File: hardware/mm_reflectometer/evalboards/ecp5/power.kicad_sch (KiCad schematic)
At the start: 49 parts, among them U101 ECP5U_25_CABGA256, U201 TLV70025_WSON6, U202 TLV62569DRL, U203 TLV62569DRL, U204 TLV70018_WSON6, U205 LM3880MF-1AF, U206 LT3494

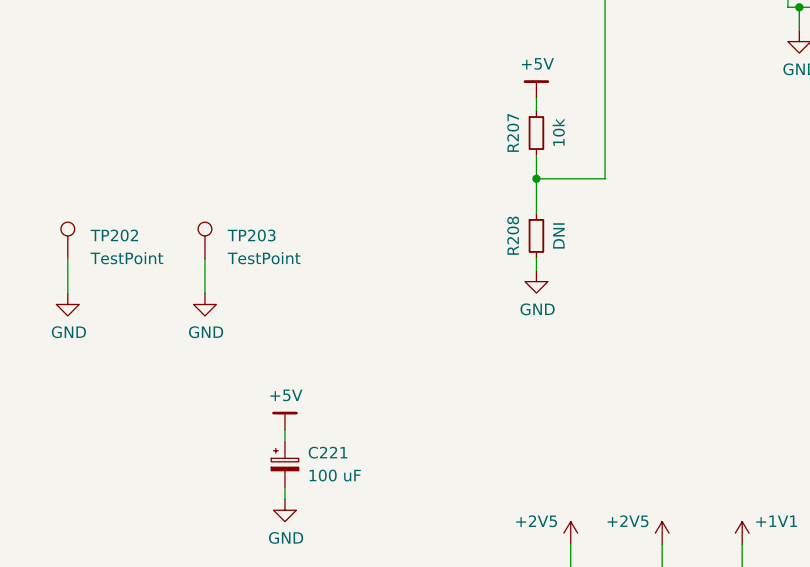
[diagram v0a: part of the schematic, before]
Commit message: all nets routed on ecp5 eval board
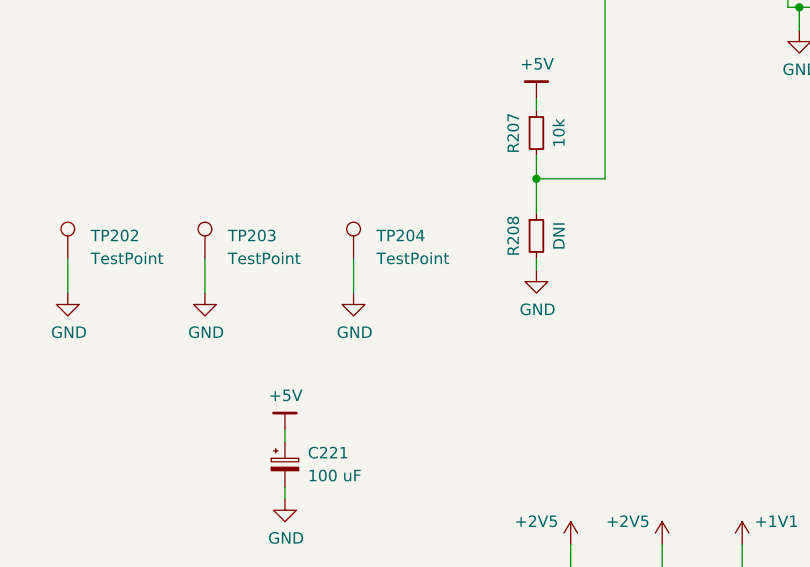
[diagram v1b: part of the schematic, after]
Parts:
- added TP204: TestPoint, TestPoint:TestPoint_Keystone_5015_Micro-Minature, symbol Connector:TestPoint
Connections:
- net GND: now also TP204.1
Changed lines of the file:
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@@
+    (stroke (width 0) (type solid) (color 0 0 0 0))
+  )
+  (wire (pts (xy 181.61 80.01) (xy 181.61 83.82))
     (stroke (width 0) (type solid) (color 0 0 0 0))
   )
@@
     )
   )
+  (symbol (lib_id "Connector:TestPoint") (at 181.61 80.01 0) (unit 1)
+    (in_bom yes) (on_board yes)
+    (property "Reference" "TP204" (id 0) (at 184.15 77.47 0)
+      (effects (font (size 1.27 1.27)) (justify left))
+    )
+    (property "Value" "TestPoint" (id 1) (at 184.15 80.01 0)
+      (effects (font (size 1.27 1.27)) (justify left))
+    )
+    (property "Footprint" "TestPoint:TestPoint_Keystone_5015_Micro-Minature" (id 2) (at 186.69 80.01 0)
+      (effects (font (size 1.27 1.27)) hide)
+    )
+    (property "Datasheet" "~" (id 3) (at 186.69 80.01 0)
+      (effects (font (size 1.27 1.27)) hide)
+    )
+  )
   (symbol (lib_id "power:+3V3") (at 26.67 52.07 0) (unit 1)
     (in_bom yes) (on_board yes)
@@
       (effects (font (size 1.27 1.27)) hide)
     )
+  )
+  (symbol (lib_id "power:GND") (at 181.61 83.82 0) (unit 1)
+    (in_bom yes) (on_board yes)
+    (property "Reference" "#PWR0245" (id 0) (at 181.61 90.17 0)
+      (effects (font (size 1.27 1.27)) hide)
+    )
+    (property "Value" "GND" (id 1) (at 181.737 88.2142 0))
+    (property "Footprint" "" (id 2) (at 181.61 83.82 0)
+      (effects (font (size 1.27 1.27)) hide)
+    )
+    (property "Datasheet" "" (id 3) (at 181.61 83.82 0)
+      (effects (font (size 1.27 1.27)) hide)
+    )

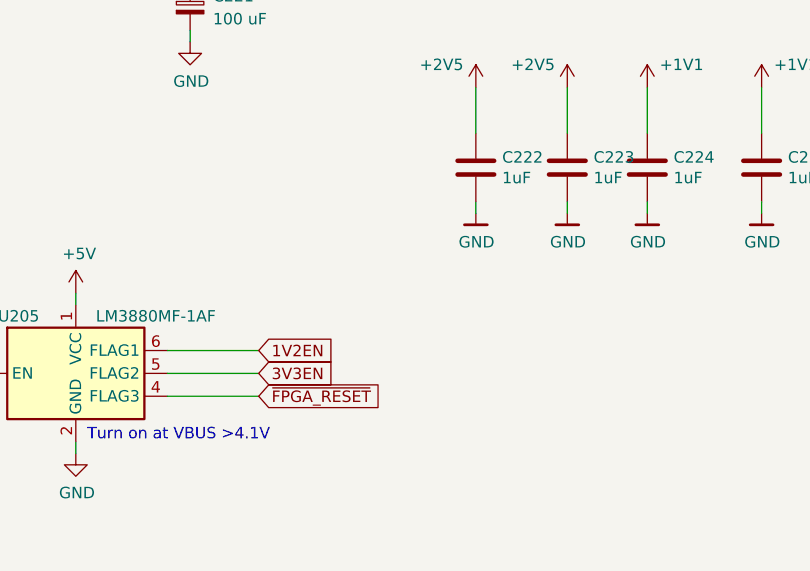
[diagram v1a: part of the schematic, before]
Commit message: cleanup ecp5 schematic, generated assembly drawings
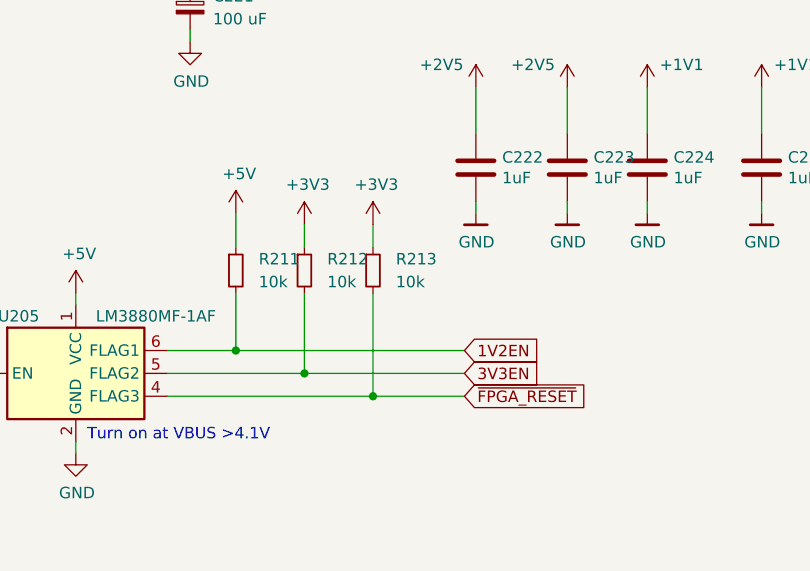
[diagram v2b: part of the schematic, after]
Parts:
- added R211, R212, R213: 10k, Resistor_SMD:R_0402_1005Metric, symbol Device:R_Small
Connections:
- net +3V3: now also R212.1, R213.1
- net +5V: now also R211.1
- net 1V2EN: now also R211.2
- net 3V3EN: now also R212.2
- net ~FPGA_RESET: now also R213.2
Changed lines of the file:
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@@
   (junction (at 153.67 34.29) (diameter 0.9144) (color 0 0 0 0))
   (junction (at 177.8 34.29) (diameter 0.9144) (color 0 0 0 0))
+  (junction (at 179.07 140.97) (diameter 0.9144) (color 0 0 0 0))
   (junction (at 186.69 34.29) (diameter 0.9144) (color 0 0 0 0))
+  (junction (at 186.69 143.51) (diameter 0.9144) (color 0 0 0 0))
+  (junction (at 194.31 146.05) (diameter 0.9144) (color 0 0 0 0))
   (junction (at 196.85 34.29) (diameter 0.9144) (color 0 0 0 0))
   (junction (at 201.93 71.12) (diameter 0.9144) (color 0 0 0 0))
@@
     (stroke (width 0) (type solid) (color 0 0 0 0))
   )
-  (wire (pts (xy 171.45 140.97) (xy 181.61 140.97))
-    (stroke (width 0) (type solid) (color 0 0 0 0))
-  )
-  (wire (pts (xy 171.45 143.51) (xy 181.61 143.51))
-    (stroke (width 0) (type solid) (color 0 0 0 0))
-  )
-  (wire (pts (xy 171.45 146.05) (xy 181.61 146.05))
+  (wire (pts (xy 171.45 140.97) (xy 179.07 140.97))
+    (stroke (width 0) (type solid) (color 0 0 0 0))
+  )
+  (wire (pts (xy 171.45 143.51) (xy 186.69 143.51))
+    (stroke (width 0) (type solid) (color 0 0 0 0))
+  )
+  (wire (pts (xy 171.45 146.05) (xy 194.31 146.05))
     (stroke (width 0) (type solid) (color 0 0 0 0))
   )
@@
     (stroke (width 0) (type solid) (color 0 0 0 0))
   )
+  (wire (pts (xy 179.07 125.73) (xy 179.07 129.54))
+    (stroke (width 0) (type solid) (color 0 0 0 0))
+  )
+  (wire (pts (xy 179.07 134.62) (xy 179.07 140.97))
+    (stroke (width 0) (type solid) (color 0 0 0 0))
+  )
+  (wire (pts (xy 179.07 140.97) (xy 204.47 140.97))
+    (stroke (width 0) (type solid) (color 0 0 0 0))
+  )
   (wire (pts (xy 181.61 80.01) (xy 181.61 83.82))
     (stroke (width 0) (type solid) (color 0 0 0 0))
@@
   )
   (wire (pts (xy 186.69 41.91) (xy 186.69 45.72))
+    (stroke (width 0) (type solid) (color 0 0 0 0))
+  )
+  (wire (pts (xy 186.69 127) (xy 186.69 129.54))
+    (stroke (width 0) (type solid) (color 0 0 0 0))
+  )
+  (wire (pts (xy 186.69 134.62) (xy 186.69 143.51))
+    (stroke (width 0) (type solid) (color 0 0 0 0))
+  )
+  (wire (pts (xy 186.69 143.51) (xy 204.47 143.51))
+    (stroke (width 0) (type solid) (color 0 0 0 0))
+  )
+  (wire (pts (xy 194.31 127) (xy 194.31 129.54))
+    (stroke (width 0) (type solid) (color 0 0 0 0))
+  )
+  (wire (pts (xy 194.31 134.62) (xy 194.31 146.05))
+    (stroke (width 0) (type solid) (color 0 0 0 0))
+  )
+  (wire (pts (xy 194.31 146.05) (xy 204.47 146.05))
     (stroke (width 0) (type solid) (color 0 0 0 0))
   )
@@
     (effects (font (size 1.27 1.27)) (justify right))
   )
-  (global_label "1V2EN" (shape input) (at 181.61 140.97 0)    (property "Intersheet References" "${INTERSHEET_REFS}" (id 0) (at 251.46 218.44 0)
+  (global_label "1V2EN" (shape input) (at 204.47 140.97 0)    (property "Intersheet References" "${INTERSHEET_REFS}" (id 0) (at 274.32 218.44 0)
       (effects (font (size 1.27 1.27)) hide)
     )
     (effects (font (size 1.27 1.27)) (justify left))
   )
-  (global_label "3V3EN" (shape input) (at 181.61 143.51 0)    (property "Intersheet References" "${INTERSHEET_REFS}" (id 0) (at 251.46 223.52 0)
+  (global_label "3V3EN" (shape input) (at 204.47 143.51 0)    (property "Intersheet References" "${INTERSHEET_REFS}" (id 0) (at 274.32 223.52 0)
       (effects (font (size 1.27 1.27)) hide)
     )
     (effects (font (size 1.27 1.27)) (justify left))
   )
-  (global_label "~FPGA_RESET" (shape input) (at 181.61 146.05 0)    (property "Intersheet References" "${INTERSHEET_REFS}" (id 0) (at 196.9771 145.9706 0)
+  (global_label "~FPGA_RESET" (shape input) (at 204.47 146.05 0)    (property "Intersheet References" "${INTERSHEET_REFS}" (id 0) (at 219.8371 145.9706 0)
       (effects (font (size 1.27 1.27)) (justify left) hide)
     )
@@
     )
   )
+  (symbol (lib_id "power:+5V") (at 179.07 125.73 0) (unit 1)
+    (in_bom yes) (on_board yes)
+    (property "Reference" "#PWR0284" (id 0) (at 179.07 129.54 0)
+      (effects (font (size 1.27 1.27)) hide)
+    )
+    (property "Value" "+5V" (id 1) (at 179.451 121.3358 0))
+    (property "Footprint" "" (id 2) (at 179.07 125.73 0)
+      (effects (font (size 1.27 1.27)) hide)
+    )
+    (property "Datasheet" "" (id 3) (at 179.07 125.73 0)
+      (effects (font (size 1.27 1.27)) hide)
+    )
+  )
+  (symbol (lib_id "power:+3V3") (at 186.69 127 0) (unit 1)
+    (in_bom yes) (on_board yes)
+    (property "Reference" "#PWR0285" (id 0) (at 186.69 130.81 0)
+      (effects (font (size 1.27 1.27)) hide)
+    )
+    (property "Value" "+3V3" (id 1) (at 187.071 122.5296 0))
+    (property "Footprint" "" (id 2) (at 186.69 127 0)
+      (effects (font (size 1.27 1.27)) hide)
+    )
+    (property "Datasheet" "" (id 3) (at 186.69 127 0)
+      (effects (font (size 1.27 1.27)) hide)
+    )
+  )
+  (symbol (lib_id "power:+3V3") (at 194.31 127 0) (unit 1)
+    (in_bom yes) (on_board yes)
+    (property "Reference" "#PWR0279" (id 0) (at 194.31 130.81 0)
+      (effects (font (size 1.27 1.27)) hide)
+    )
+    (property "Value" "+3V3" (id 1) (at 194.691 122.5296 0))
+    (property "Footprint" "" (id 2) (at 194.31 127 0)
+      (effects (font (size 1.27 1.27)) hide)
+    )
+    (property "Datasheet" "" (id 3) (at 194.31 127 0)
+      (effects (font (size 1.27 1.27)) hide)
+    )
+  )
   (symbol (lib_id "power:+2V5") (at 205.74 111.76 0) (mirror y) (unit 1)
     (in_bom yes) (on_board yes)
@@
       (effects (font (size 1.27 1.27)) hide)
     )
+  )
+  (symbol (lib_id "Device:R_Small") (at 179.07 132.08 0) (unit 1)
+    (in_bom yes) (on_board yes)
+    (property "Reference" "R211" (id 0) (at 181.61 130.81 0)
+      (effects (font (size 1.27 1.27)) (justify left))
+    )
+    (property "Value" "10k" (id 1) (at 181.61 133.35 0)
+      (effects (font (size 1.27 1.27)) (justify left))
+    )
+    (property "Footprint" "Resistor_SMD:R_0402_1005Metric" (id 2) (at 179.07 132.08 0)
+      (effects (font (size 1.27 1.27)) hide)
+    )
+    (property "Datasheet" "~" (id 3) (at 179.07 132.08 0)
+      (effects (font (size 1.27 1.27)) hide)
+    )
+  )
+  (symbol (lib_id "Device:R_Small") (at 186.69 132.08 0) (unit 1)
+    (in_bom yes) (on_board yes)
+    (property "Reference" "R212" (id 0) (at 189.23 130.81 0)
+      (effects (font (size 1.27 1.27)) (justify left))
+    )
+    (property "Value" "10k" (id 1) (at 189.23 133.35 0)
+      (effects (font (size 1.27 1.27)) (justify left))
+    )
+    (property "Footprint" "Resistor_SMD:R_0402_1005Metric" (id 2) (at 186.69 132.08 0)
+      (effects (font (size 1.27 1.27)) hide)
+    )
+    (property "Datasheet" "~" (id 3) (at 186.69 132.08 0)
+      (effects (font (size 1.27 1.27)) hide)
+    )
+  )
+  (symbol (lib_id "Device:R_Small") (at 194.31 132.08 0) (unit 1)
+    (in_bom yes) (on_board yes)
+    (property "Reference" "R213" (id 0) (at 196.85 130.81 0)
+      (effects (font (size 1.27 1.27)) (justify left))
+    )
+    (property "Value" "10k" (id 1) (at 196.85 133.35 0)
+      (effects (font (size 1.27 1.27)) (justify left))
+    )
+    (property "Footprint" "Resistor_SMD:R_0402_1005Metric" (id 2) (at 194.31 132.08 0)
+      (effects (font (size 1.27 1.27)) hide)
+    )
+    (property "Datasheet" "~" (id 3) (at 194.31 132.08 0)
+      (effects (font (size 1.27 1.27)) hide)
+    )

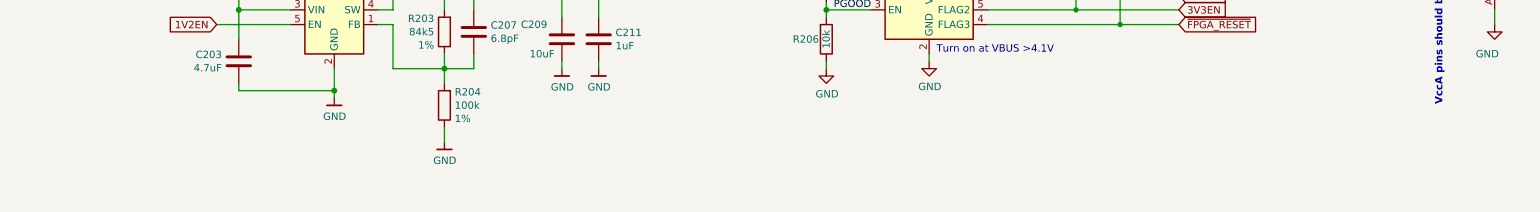
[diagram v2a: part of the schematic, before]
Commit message: fixed maam-011101 eval board pinout, started bringup of ecp5 board
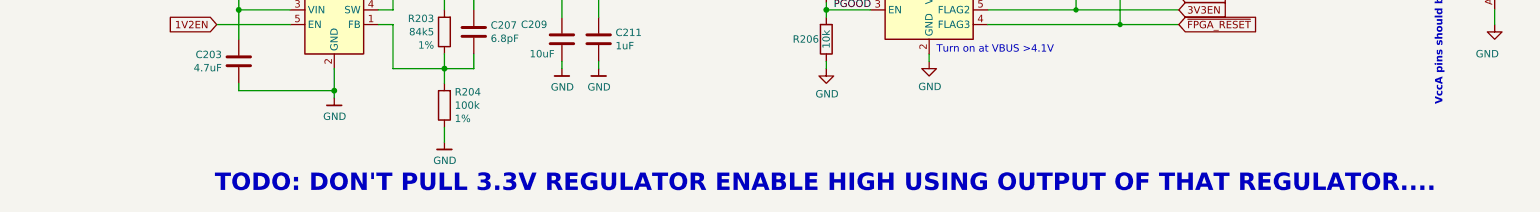
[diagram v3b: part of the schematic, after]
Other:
- note added: "TODO: DON'T PULL 3.3V REGULATOR ENABLE HIGH USING OUTPUT OF THAT REGULATOR...."
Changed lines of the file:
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@@
     (effects (font (size 1.27 1.27)) (justify left bottom))
+  )
+  (text "TODO: DON'T PULL 3.3V REGULATOR ENABLE HIGH USING OUTPUT OF THAT REGULATOR...."
+    (at 248.92 175.26 0)
+    (effects (font (size 3 3) (thickness 0.6) bold) (justify right bottom))
   )
   (text "VccA pins should be isolated from Vcc and switching regulator noise if serdes is used!"
